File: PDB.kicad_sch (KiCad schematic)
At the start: 32 parts, among them U13 B6B-XH-A(LF)(SN), U13 INA240A1QDRQ1, U14 TPS62933DRLR, U15 53.6k

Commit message: GPS connections made
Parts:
- removed C33: 100nF 25v, easyeda2kicad:C0402, symbol easyeda2kicad:CL05A104KA5NNNC
- removed C33, C34: 10uF 25v, easyeda2kicad:C0603, symbol easyeda2kicad:ZRB18AR61E106ME01L
- removed R27: 22k, easyeda2kicad:R0603, symbol easyeda2kicad:RT0603BRD0722KL
- removed R5: 100k, easyeda2kicad:R0603, symbol easyeda2kicad:RT0603BRD07100KL
- added C31, C33: 10uF, PCM_JLCPCB:C_0805, symbol PCM_JLCPCB-Capacitors:0805,10uF,(2)
- added C36: 100nF, PCM_JLCPCB:C_0402, symbol PCM_JLCPCB-Capacitors:0402,100nF,(2)
- added R21: 10kΩ, PCM_JLCPCB:R_0402, symbol PCM_JLCPCB-Resistors:0402,10kΩ
- added R6: 75kΩ, PCM_JLCPCB:R_0402, symbol PCM_JLCPCB-Resistors:0402,75kΩ
- added TP29: 5V_test, symbol Connector:TestPoint
- added TP30: GND, symbol Connector:TestPoint
- LED1: value KT-0603R -> SYS_PWR_ON
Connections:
- net 5V_VBAT: now also TP29.1
- net CURRENT_SCALED: now also U13.4; no longer U13.6
- net CURR_IN: now also R6.1
- net CURR_OUT: now also C31.1, C33.1, C36.1; no longer U14.2 (EN)
- net GND: now also U13.5, U13.6, C31.2, C33.2, C36.2, R21.2, TP30.1; no longer U13.3, U13.4
- net VBAT_SCALED: now also U13.3; no longer U13.5
- net at L3.1, U14.5 (SW): now also C38.2; no longer C38.1
- net at D5.1 (K): now also R21.1, R6.2
- net at U14.6 (BST): now also C38.1; no longer C38.2
- no-connect marks 2 -> 11
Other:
- note added: "2S(7.4v) to 6S(25.2V)"
- note added: "2S-6S / 5V,3A BUCK REGULATOR"
- note added: "6-25.5V -> 0.71-3V"
- note added: "ESC POWER SUPPLY PADS"
- note removed: "2S(7.4v) to 4S(14.8V)"
- note removed: "2S-4S / 5V,3A BUCK REGULATOR"
- note removed: "ESC SUPPLY PADS"
- moved on the sheet: C29, C30, C34, C35, C38, C39, D5, L3, LED1, R26, R28, R29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

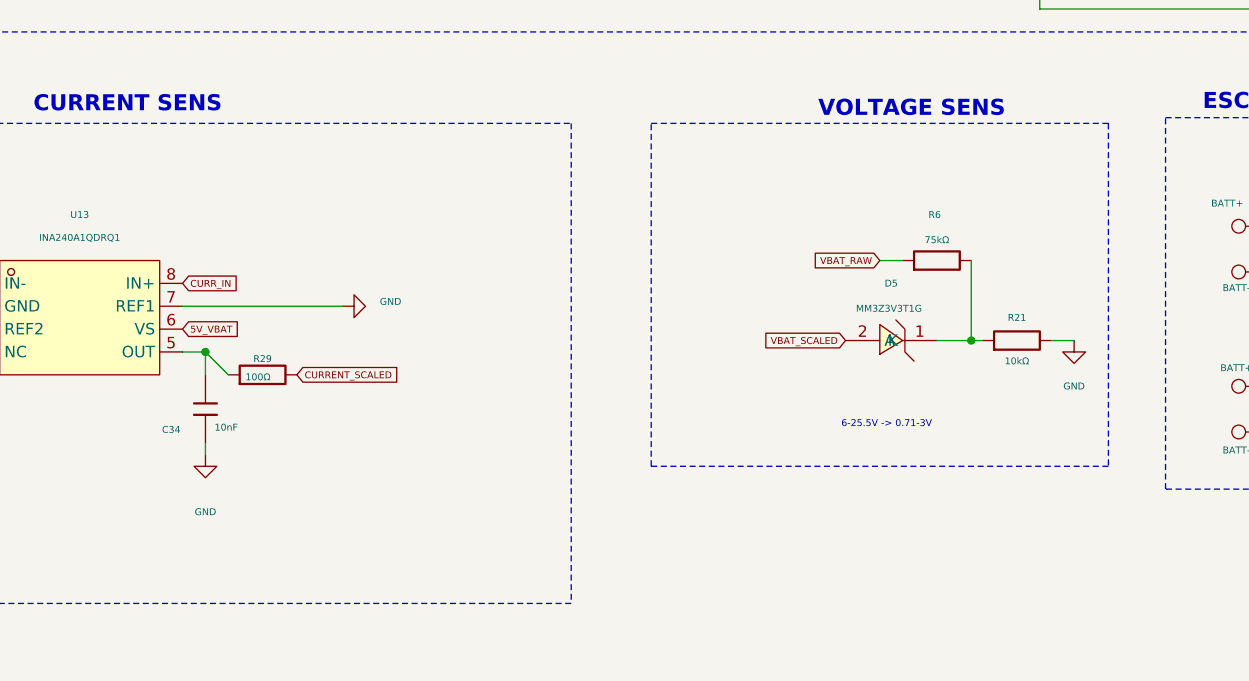
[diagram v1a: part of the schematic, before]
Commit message: corrected current sens and voltage sens to filter scaled current reading using RC filter and clamp voltage to 3.3 in case of over voltage respectiveley
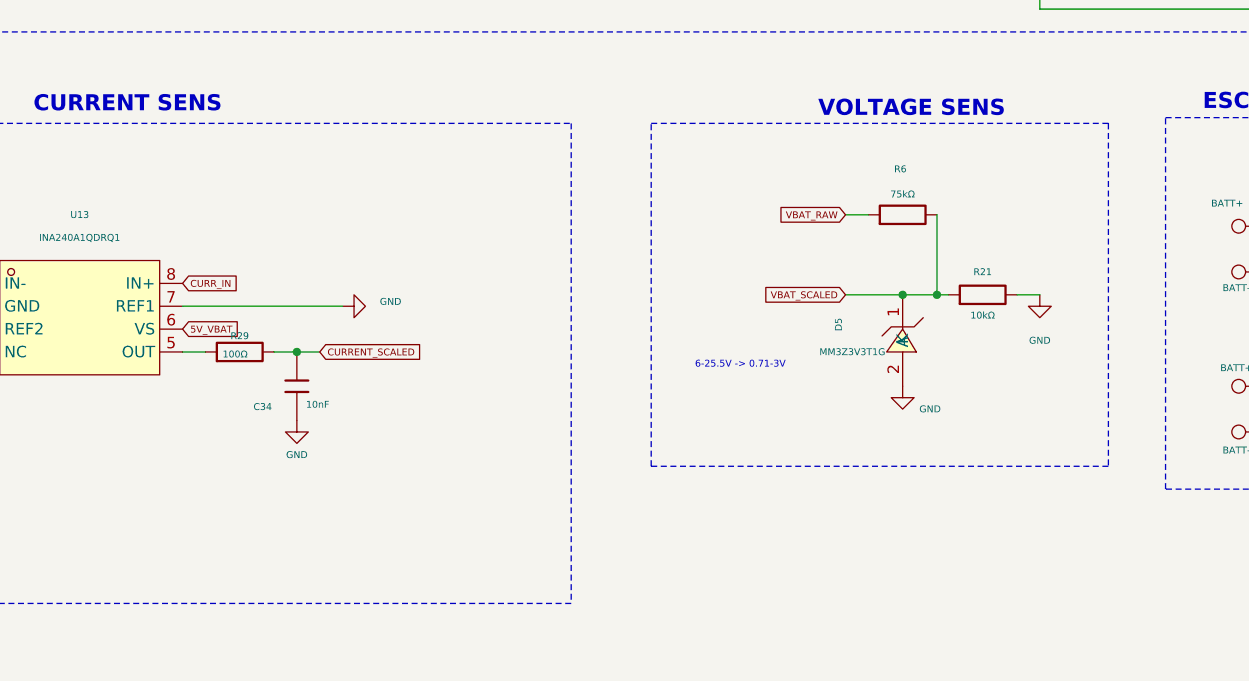
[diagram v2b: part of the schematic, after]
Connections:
- net CURRENT_SCALED: now also C34.2
- net GND: now also D5.2 (A)
- net VBAT_SCALED: now also D5.1 (K), R21.1, R6.2; no longer D5.2 (A)
- net at R29.1, U13.5 (OUT): no longer C34.2
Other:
- moved on the sheet: C34, D5, R21, R29, R6

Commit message: Added PWR flags, Changed MCU pins electrical characteristics to bidirectional, rectified some ERC errors
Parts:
- renumbered C33 to C32, C31 to C33, C36 to C35, C39 to C36, C38 to C37, C29 to C38, C30 to C39, C35 to C40, D5 to D4, L3 to L2, LED1 to LED5, R28 to R20, R29 to R21, R6 to R22, R21 to R23, R26 to R24, R28 to R25, TP12 to TP19, TP13 to TP20, TP14 to TP21, TP25 to TP23, TP26 to TP24, TP23 to TP25, TP24 to TP26, U13 to U11, U14 to U12, U15 to U13, U13 to U14

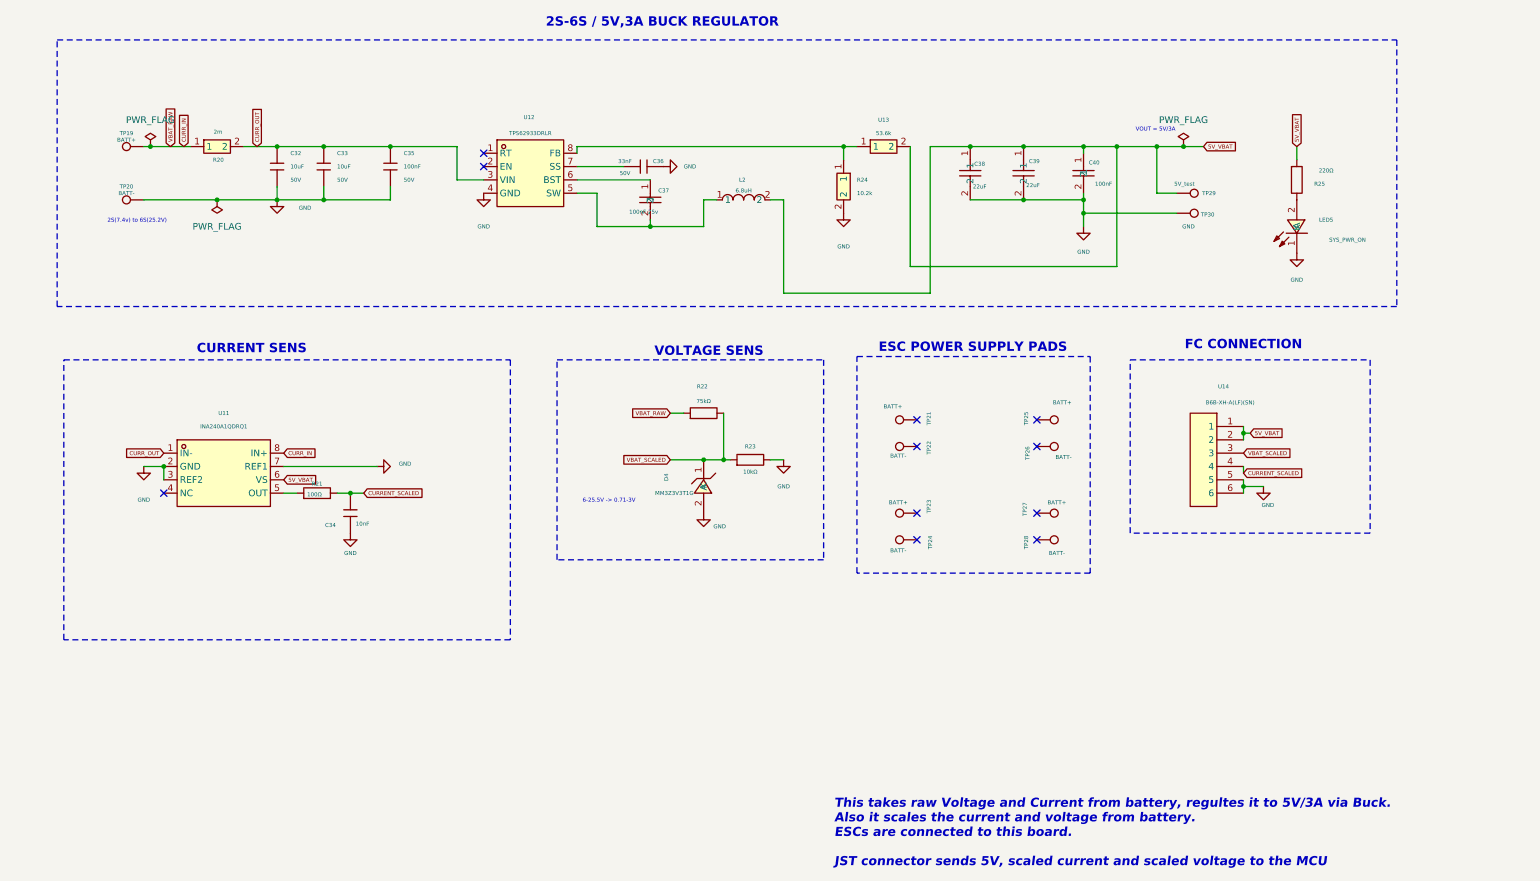
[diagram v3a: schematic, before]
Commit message: Assigned proper footprints, Re-annotated, Connection modification for efficient PCB layout, First PCB update
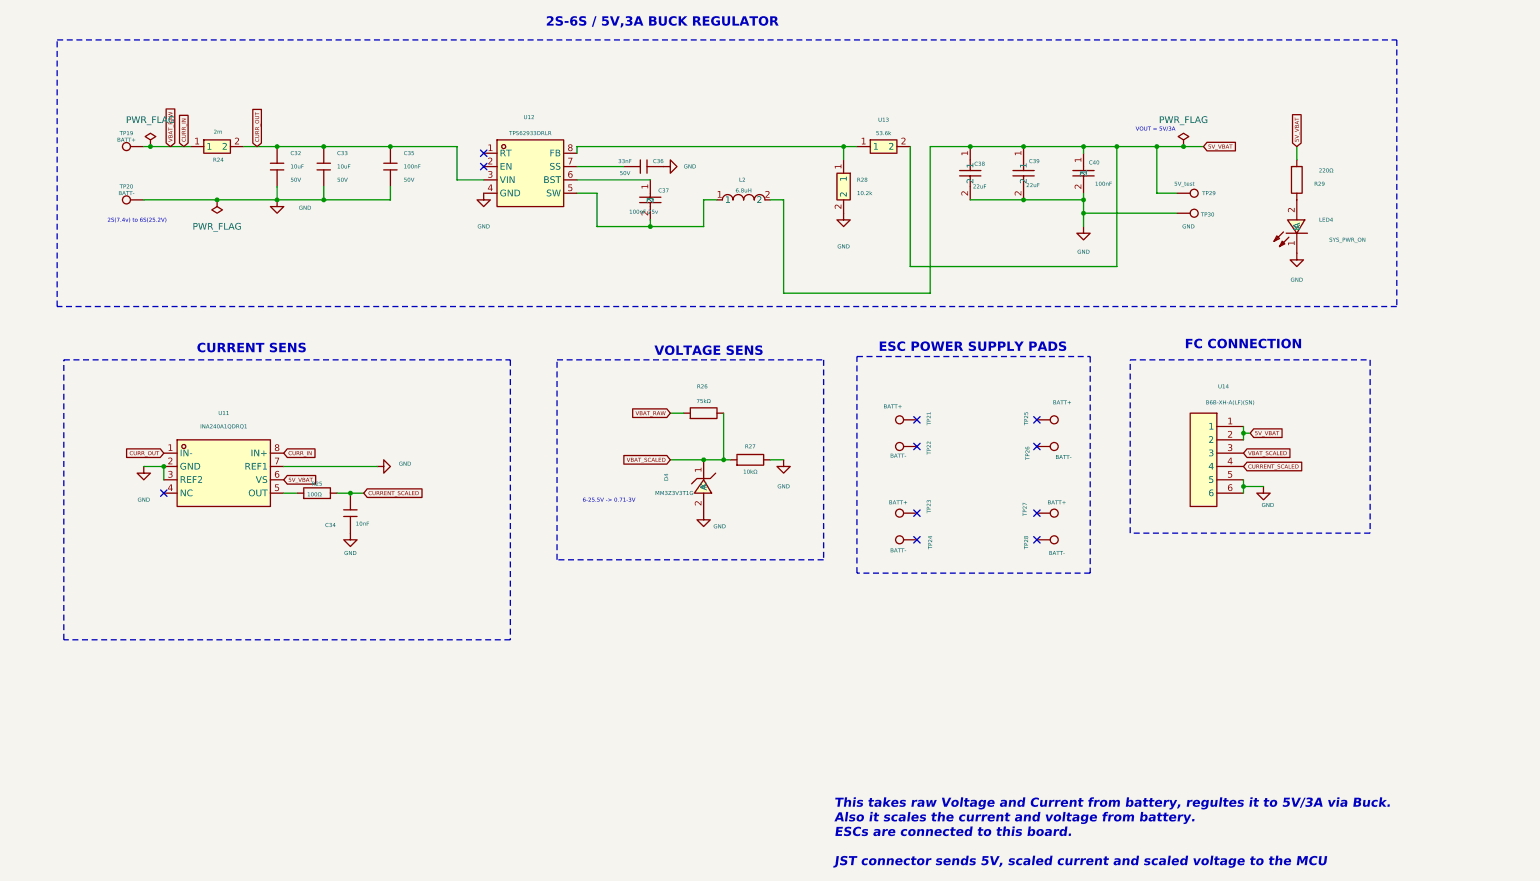
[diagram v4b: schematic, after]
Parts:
- C32, C33: footprint PCM_JLCPCB:C_0805 -> easyeda2kicad:C0805
- C34, C35: footprint PCM_JLCPCB:C_0402 -> easyeda2kicad:C0402
- C36: footprint PCM_JLCPCB:C_0603 -> easyeda2kicad:C0603
- R25: renamed from R21; footprint PCM_JLCPCB:R_0402 -> easyeda2kicad:R0402
- R26: renamed from R22; footprint PCM_JLCPCB:R_0402 -> easyeda2kicad:R0402
- R27: renamed from R23; footprint PCM_JLCPCB:R_0402 -> easyeda2kicad:R0402
- R29: renamed from R25; footprint PCM_JLCPCB:R_0603 -> easyeda2kicad:R0603
- TP19, TP20, TP21, TP22, TP23, TP24, TP25, TP26, TP27, TP28, TP30: footprint (none) -> TestPoint:TestPoint_Pad_4.0x4.0mm
- TP29: footprint (none) -> TestPoint:TestPoint_Pad_D2.0mm
- renumbered LED5 to LED4, R20 to R24, R24 to R28

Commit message: Joind PDB Batt+ and Batt- pads to LiPo battery input net
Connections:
- net CURR_IN: now also TP21.1, TP23.1, TP25.1, TP27.1
- net GND: now also TP22.1, TP24.1, TP26.1, TP28.1
- no-connect marks 11 -> 3
